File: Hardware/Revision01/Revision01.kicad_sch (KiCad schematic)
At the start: 29 parts, among them J1 Battery connector, SW2 SW_SPST_LED, U10 NCP1117LPST50T3G

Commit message: random stuff added
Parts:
- added H4: MountingHole, MountingHole:MountingHole_3.2mm_M3, symbol Mechanical:MountingHole
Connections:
- net PC5_GPIO: no longer D3.1 (K), R11.1
- new net: D3.1 (K), R11.1
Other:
- note added: "PUT MOUNTING HOLE WITH CONNECTOR TO GND ON CAR"

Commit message: some feedback implemented, MISO/MOSI SIWTCHED, GPIO_USB_5V FIXED, COMMENTS REGARDING ALTERNATIVE ADC's, and PCB CONNECTED TO EXTERNAL GND added
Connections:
- no-connect marks 28 -> 27
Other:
- sheet Application ports: added ~ANT_CSCON, ~CS_DATA, ~ICM_CS, ~StrainV_Enable, ~strainGaugeCS; removed ANT_CSCON, ANT_CS_ActiveLow, ICM_CS, StrainV_Enable, strainGaugeCS
- note added: "PUT MOUNTING HOLE CONNECTED TO GND WHICH ATTACHS TO EXTERNAL GND ON CAR"
- note removed: "PUT MOUNTING HOLE WITH CONNECTOR TO GND ON CAR"

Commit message: Implemented new more reliable design utilizing instrumentation amplifiers
Changed RESISTORS for new Power requirements
Added prototype features of breathing cube to test out.
Removed MCU sheet, as moving pins around was getting too messy
Picked out Instrumentation OP-AMP, INA331 or INA2331
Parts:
- added TP60, TP63, TP64, TP65: TestPoint, TestPoint:TestPoint_Pad_D1.5mm, symbol Connector:TestPoint
- added U3: NUCLEO-L476RG, NUCLEO-L476RG:MODULE_NUCLEO-L476RG, symbol NUCLEO-L476RG:NUCLEO-L476RG
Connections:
- net +3.3V: now also U3.CN7_16 (+3V3)
- net +5V: now also U3.CN7_18 (+5V)
- net +5V_USB: now also U3.CN10_8 (U5V)
- net ANT_IRQ0_GPIO: now also U3.CN10_15 (PA7)
- net ANT_IRQ1_GPIO: now also U3.CN10_17 (PB6)
- net ANT_RESET_ANT_GPIO: now also U3.CN10_19 (PC7)
- net GND: now also U3.CN10_20 (GND_CN10_20), U3.CN10_32 (AGND), U3.CN10_9 (GND_CN10_9), U3.CN7_19 (GND_CN7_19), U3.CN7_20 (GND_CN7_20), U3.CN7_22 (GND_CN7_22), U3.CN7_8 (GND_CN7_8)
- net ICM_CS_GPIO: now also U3.CN10_6 (PC5)
- net ICM_INT1_GPIO: now also U3.CN10_2 (PC8)
- net ICM_INT2_GPIO: now also U3.CN10_4 (PC6)
- net PB13_SPI2_SCK: now also U3.CN10_30 (PB13)
- net PB14_SPI2_MISO: now also U3.CN10_28 (PB14)
- net PB15_SPI2_MOSI: now also U3.CN10_26 (PB15)
- new net: TP63.1, U3.CN7_7 (BOOT0)
- new net AIN_1: U3.CN7_38 (PC0)
- new net AIN_2: U3.CN7_36 (PC1)
- new net AIN_3: U3.CN7_35 (PC2)
- new net AIN_4: U3.CN7_37 (PC3)
- new net AIN_5: U3.CN7_28 (PA0)
- new net AIN_6: U3.CN7_30 (PA1)
- new net AIN_7: U3.CN10_35 (PA2)
- new net AIN_8: U3.CN10_37 (PA3)
- new net ANT_CSCON_GPIO: U3.CN10_11 (PA5)
- new net ANT_CSDATA_GPIO: U3.CN10_13 (PA6)
- new net AVDD_NUCLEO: U3.CN10_7 (AVDD)
- new net BatteryV_AIN: U3.CN7_32 (PA4)
- new net E5V_NUCLEO: U3.CN7_6 (E5V)
- new net I2C_SCL: U3.CN10_3 (PB8)
- new net I2C_SDA: U3.CN10_1 (PC9)
- new net IOREF: U3.CN7_12 (IOREF)
- new net LP5813_EN_GPIO: U3.CN10_5 (PB9)
- new net PA13/JTMS-SWDIO/IR_OUT: TP64.1, U3.CN7_13 (PA13)
- new net PA14/JTCK-SWCLK: TP65.1, U3.CN7_15 (PA14)
- new net PB3/JTDO-TRACESWO/TIM2_CH2/SPI1_SCK/SPI3_SCK/USART1_RTS_DE/COMP2_INM: TP60.1, U3.CN10_31 (PB3)
- new net PC13/RTC_TAMP1/RTC_TS/RTC_OUT/WKUP2: U3.CN7_23 (PC13)
- new net PC14/OSC32_IN: U3.CN7_25 (PC14)
- new net PC15/OSC32_OUT: U3.CN7_27 (PC15)
- new net PH0/OSC_IN: U3.CN7_29 (PH0)
- new net PH1/OSC_OUT: U3.CN7_31 (PH1)
- new net VBAT_PIN_NUCLEO: U3.CN7_33 (VBAT)
- new net VDD_NUCLEO: U3.CN7_5 (VDD)
- new net ~{RESET}: U3.CN7_14 (RESET)
- no-connect marks 27 -> 33
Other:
- removed sheet Controller1
- sheet Application ports: added AIN_STRAIN_1, AIN_STRAIN_2, AIN_STRAIN_3, AIN_STRAIN_4, AIN_STRAIN_5, AIN_STRAIN_6, AIN_STRAIN_7, AIN_STRAIN_8, I2C_SCL, I2C_SDA, LP5813_EN, ~{ANT_CSCON}, ~{CS_DATA}, ~{ICM_CS}, ~{StrainV_Enable}; removed ~ANT_CSCON, ~CS_DATA, ~ICM_CS, ~StrainV_Enable, ~strainGaugeCS
- note added: "(NC)"
- note added: "+3.3V <JP6> VDD"
- note added: "+3V3 = IOREF"
- note added: "10K PullDown"
- note added: "FLA of circuit is about 190mA."
- note added: "OSC32_IN"
- note added: "OSC32_OUT"
- note added: "PA5 <SB42> <SB21> LED2 (Active Hi)"
- note added: "PC13 <SB17> B1, Blue PB"
- note added: "SWCLK"
- note added: "SWDIO"
- note added: "TRACESWO"
- note added: "Table 4. Boot modes BOOT1=x | BOOT0=0 | Main Flash Memory"
- note added: "VDD"
- note added: "VDD <Bead> <SB57> AVDD"
- note added: "~{RESET} (Internal Pullup) = Black Pushbutton B2"
- note removed: "FLA of circuit is about 150mA."
- moved on the sheet: C46, C47, D3, D5, F1, J1, JP2, N1, R11, R13, SW2, U10

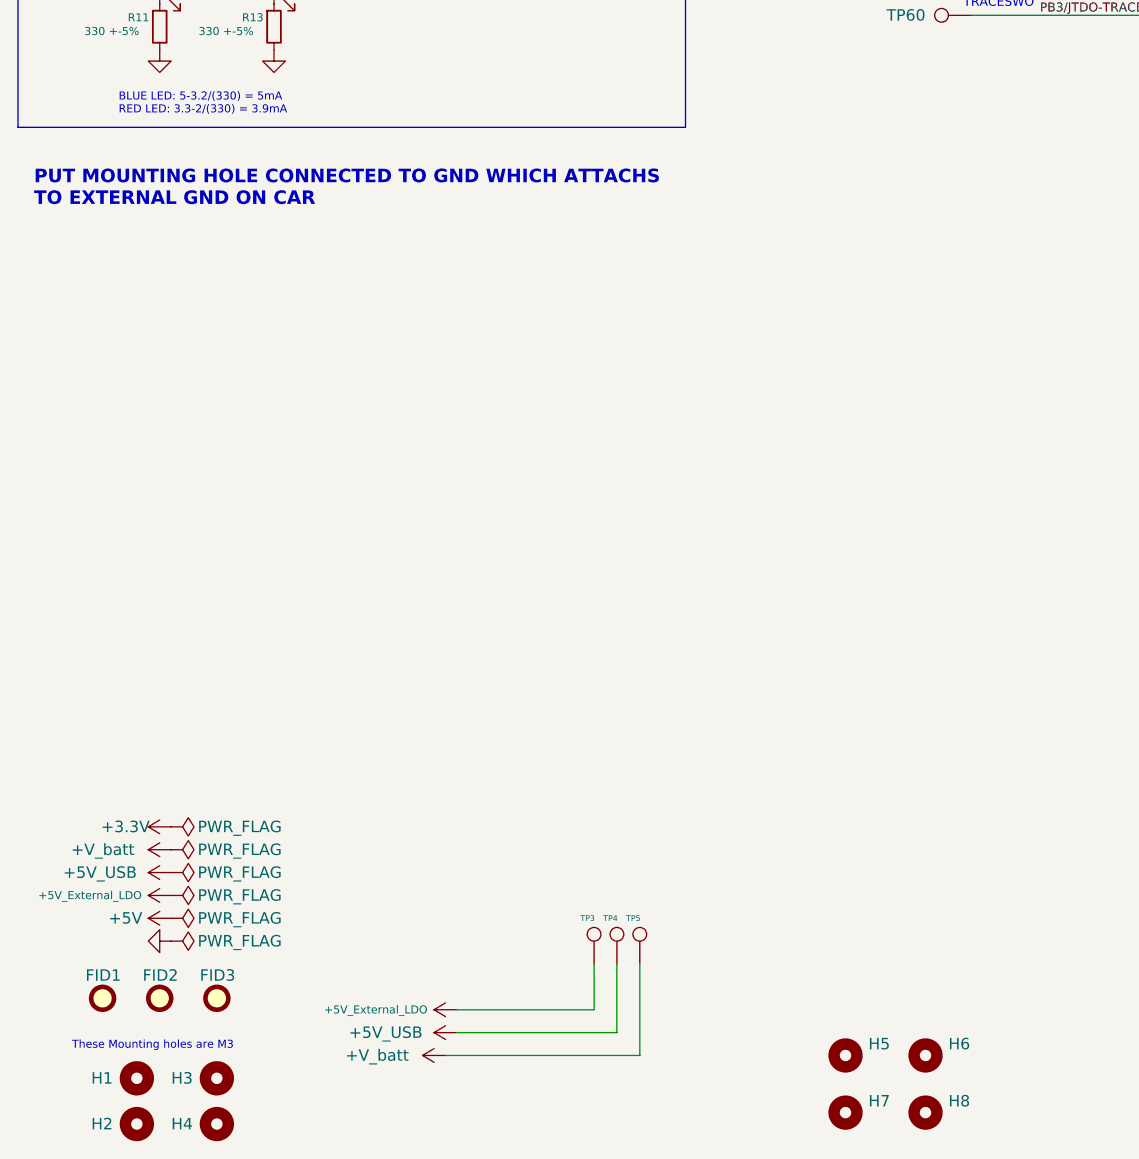
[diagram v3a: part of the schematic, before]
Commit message: Finished up small things(on schematic layout)
-Connector pins switched such that GND is pin 1
-used KICAD feature to indicate ACTIVE LOW
-polyFuse added to each StrainGauge
-Added Grounded Mounting holes connects to external GND(outside of PCB)
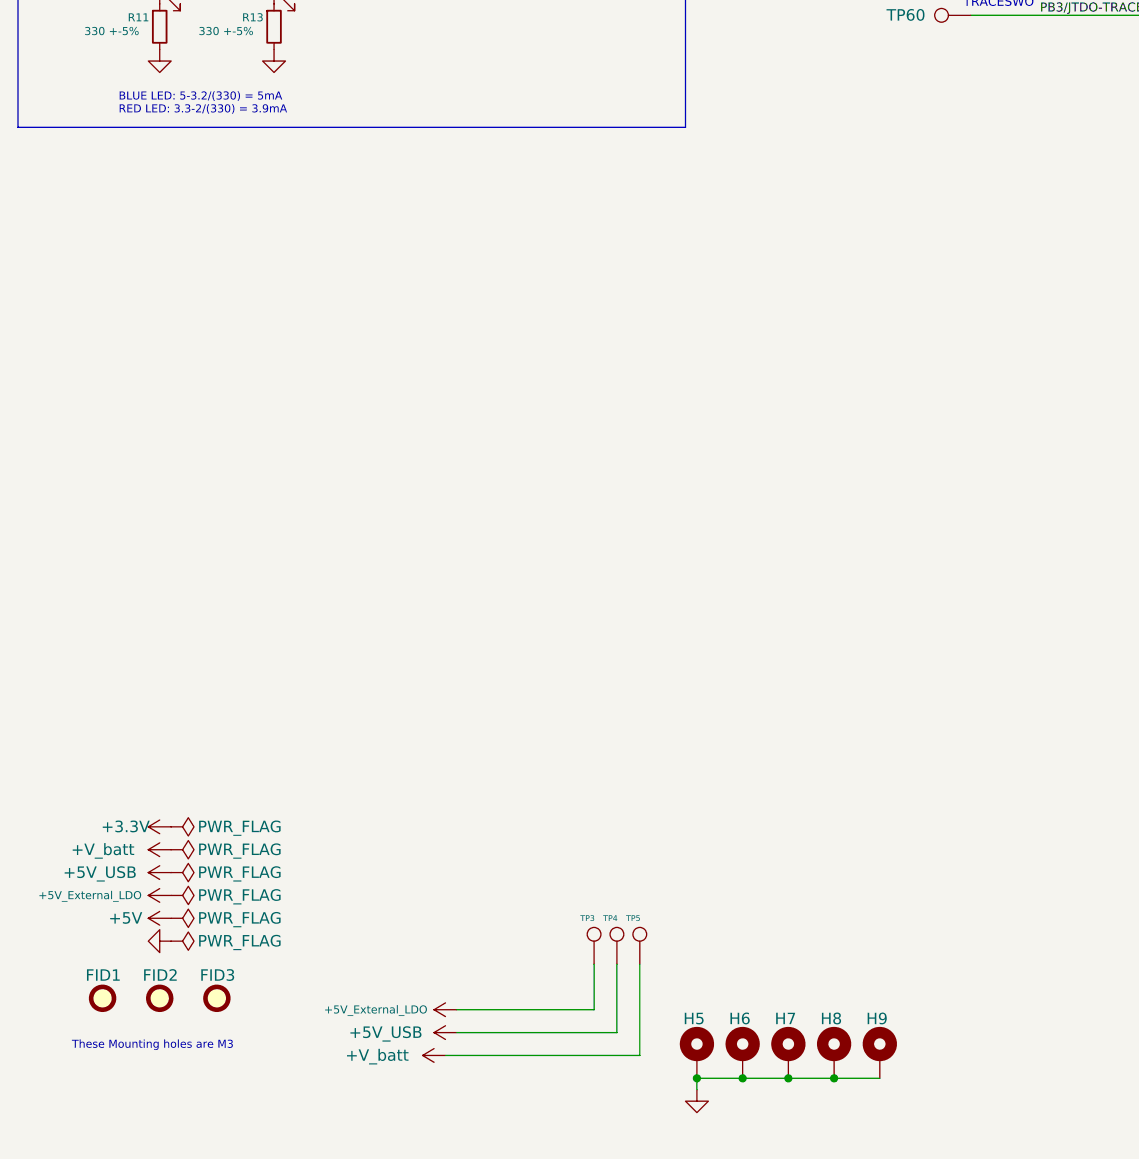
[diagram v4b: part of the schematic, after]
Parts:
- removed H1, H2, H3, H4: MountingHole, MountingHole:MountingHole_3.2mm_M3, symbol Mechanical:MountingHole
- removed H5, H6, H7, H8: MountingHole, MountingHole:MountingHole_4.3mm_M4, symbol Mechanical:MountingHole
- added H5, H6, H7, H8, H9: MountingHole_Pad_MP, symbol Mechanical:MountingHole_Pad_MP
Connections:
- net GND: now also H5.MP, H6.MP, H7.MP, H8.MP, H9.MP
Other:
- note removed: "PUT MOUNTING HOLE CONNECTED TO GND WHICH ATTACHS TO EXTERNAL GND ON CAR"

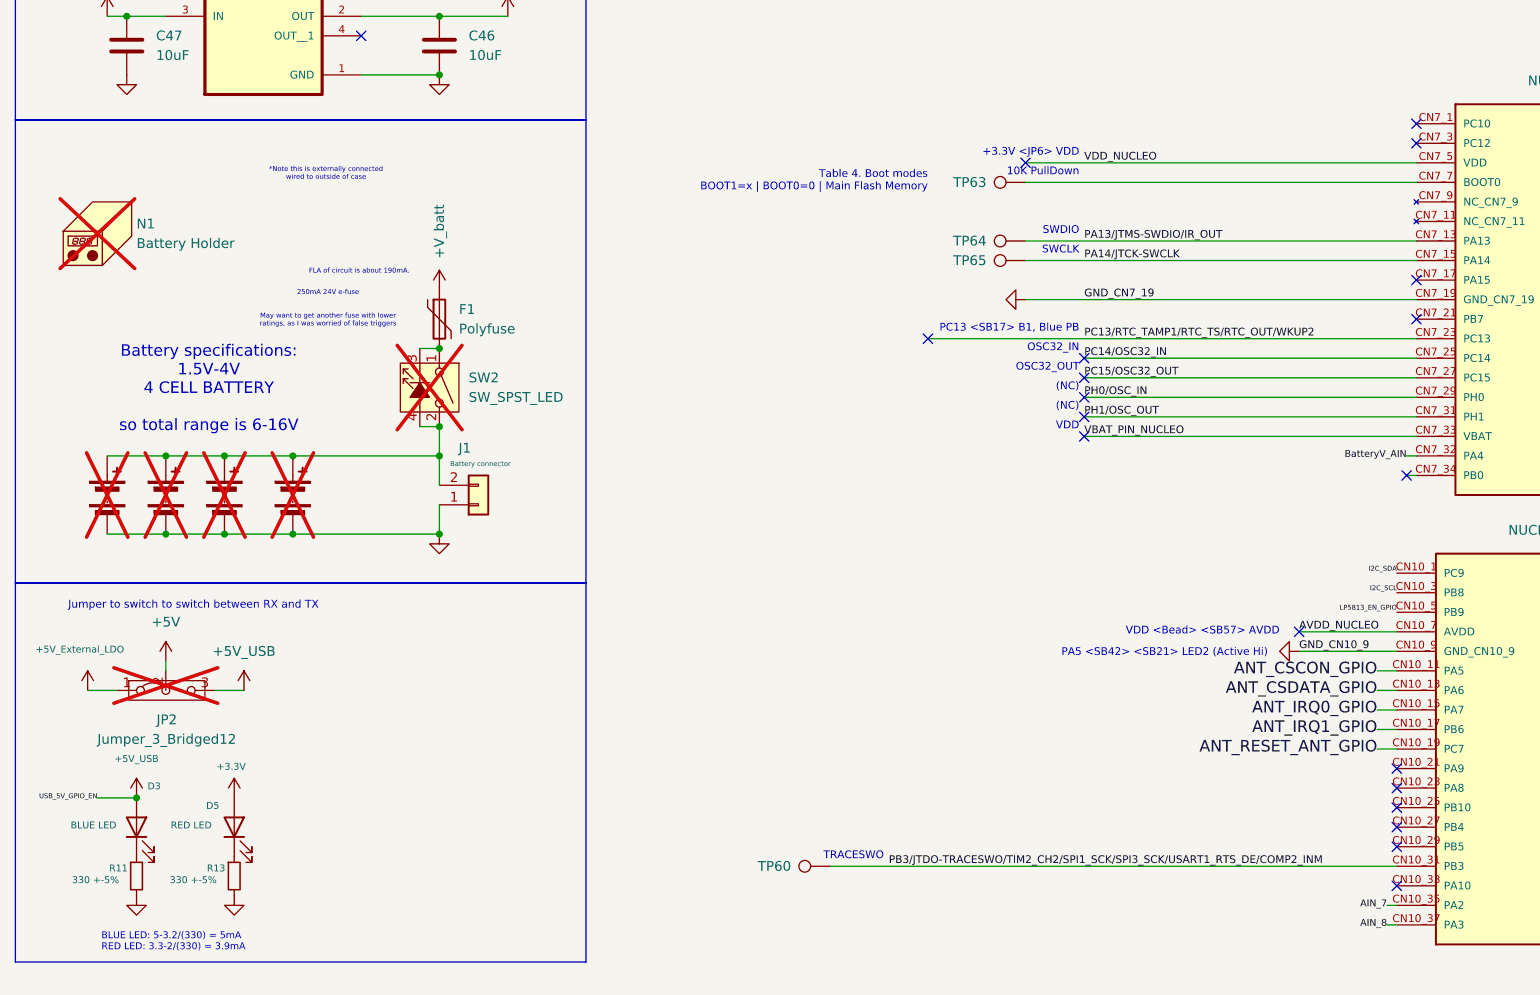
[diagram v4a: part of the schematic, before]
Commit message: I believe I have finished schematic
-Calculated RC circuit with cutoff at 10KHz for ADC
- Stimulated OP-AMP circuit with strainGauge
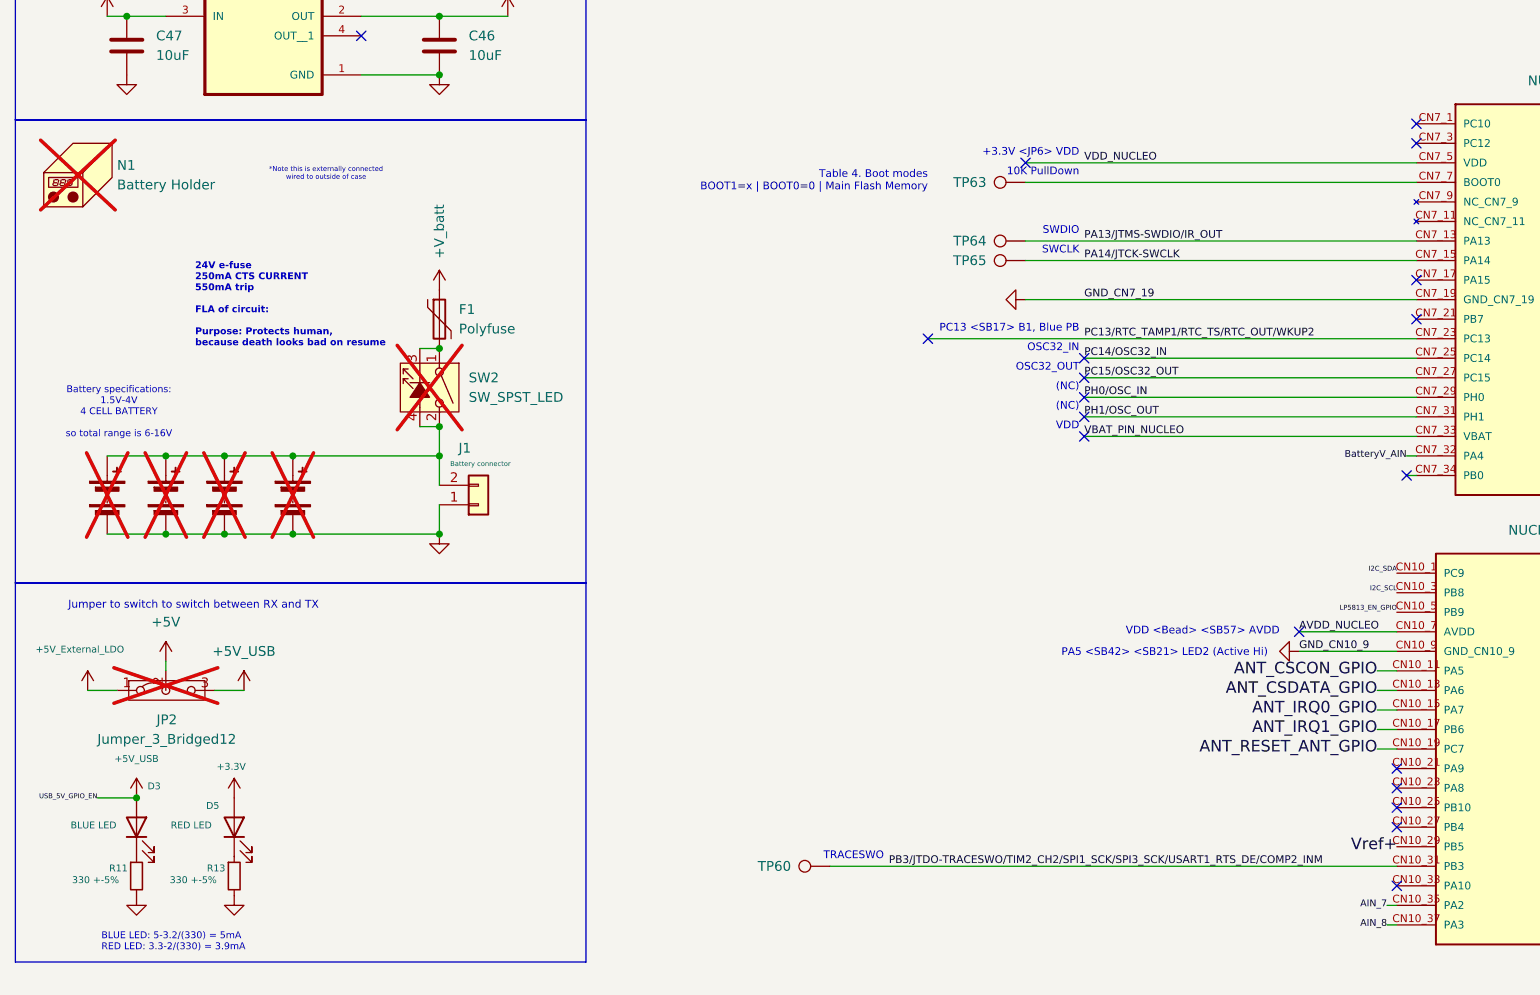
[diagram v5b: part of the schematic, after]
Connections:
- net Vref+: now reaches U3.CN10_29 (PB5)
- no-connect marks 33 -> 32
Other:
- note added: "24V e-fuse 250mA CTS CURRENT 550mA trip FLA of circuit: Purpose: Protects human, because death looks bad on resume"
- note removed: "250mA 24V e-fuse May want to get another fuse with lower ratings, as I was worried of false triggers"
- note removed: "FLA of circuit is about 190mA."
- moved on the sheet: N1
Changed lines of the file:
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@@
 		)
 	)
-	(text "FLA of circuit is about 190mA.\n"
-		(exclude_from_sim no)
-		(at 58.166 76.454 0)
-		(effects
-			(font
-				(size 0.635 0.635)
-			)
-		)
-	)
 	(text "VDD <Bead> <SB57> AVDD"
 		(exclude_from_sim no)
@@
 	(text "Battery specifications:\n1.5V-4V\n4 CELL BATTERY\n\nso total range is 6-16V"
 		(exclude_from_sim no)
-		(at 38.608 91.694 0)
+		(at 26.924 94.742 0)
 		(effects
 			(font
-				(size 1.4986 1.4986)
+				(size 0.889 0.889)
 			)
 		)
 	)
-	(text "250mA 24V e-fuse\n\n\nMay want to get another fuse with lower\nratings, as I was worried of false triggers\n"
+	(text "24V e-fuse\n250mA CTS CURRENT\n550mA trip\n\nFLA of circuit:\n\nPurpose: Protects human, \nbecause death looks bad on resume\n"
 		(exclude_from_sim no)
-		(at 54.102 81.28 0)
+		(at 36.83 80.772 0)
 		(effects
 			(font
-				(size 0.635 0.635)
+				(size 0.889 0.889)
+				(thickness 0.127)
+				(bold yes)
 			)
+			(justify left)
 		)
 	)
@@
 	)
 	(no_connect
-		(at 193.04 151.13)
-	)
-	(no_connect
 		(at 195.58 77.47)
 	)
@@
 		)
 	)
+	(label "Vref+"
+		(at 193.04 151.13 180)
+		(effects
+			(font
+				(size 1.4986 1.4986)
+			)
+			(justify right)
+		)
+	)
 	(label "PH0/OSC_IN"
 		(at 152.4 92.71 0)
@@
 	(symbol
 		(lib_id "Mechanical:Housing")
-		(at 25.4 71.12 0)
+		(at 22.86 63.5 0)
 		(unit 1)
 		(exclude_from_sim yes)
@@
 		(on_board no)
 		(dnp yes)
-		(fields_autoplaced yes)
 		(property "Reference" "N1"
-			(at 29.21 70.1674 0)
+			(at 26.67 62.5474 0)
 			(effects
 				(font
@@
 		)
 		(property "Value" "Battery Holder"
-			(at 29.21 72.7074 0)
+			(at 26.67 65.0874 0)
 			(effects
 				(font
@@
 		)
 		(property "Footprint" ""
-			(at 26.67 69.85 0)
+			(at 24.13 62.23 0)
 			(effects
 				(font
@@
 		)
 		(property "Datasheet" "~"
-			(at 26.67 69.85 0)
+			(at 24.13 62.23 0)
 			(effects
 				(font
@@
 		)
 		(property "Description" "Housing"
-			(at 25.4 71.12 0)
+			(at 22.86 63.5 0)
 			(effects
 				(font
@@
 		)
 		(property "Distributor link" "https://www.digikey.ca/en/products/detail/seeed-technology-co-ltd/114090052/10451909?s=N4IgTCBcDaIDoBcAEAhAggFQ0gEgeQBkARAUQCUkBGADgDYBWABiQBYkBhEggpAktIgGUQAXQC%2BQA"
-			(at 25.4 71.12 0)
+			(at 22.86 63.5 0)
 			(effects
 				(font
@@
 		)
 		(property "Manufacturer" "Seeed Technology Co., Ltd"
-			(at 25.4 71.12 0)
+			(at 22.86 63.5 0)
 			(effects
 				(font
@@
 		)
 		(property "Manufacturer Part Number" "114090052"
-			(at 25.4 71.12 0)
+			(at 22.86 63.5 0)
 			(effects
 				(font
@@
 		)
 		(property "Price per unit" "2.19"
-			(at 25.4 71.12 0)
+			(at 22.86 63.5 0)
 			(effects
 				(font
@@
 		)
 		(property "Quantity" "1"
-			(at 25.4 71.12 0)
+			(at 22.86 63.5 0)
 			(effects
 				(font
